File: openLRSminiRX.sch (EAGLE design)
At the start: 19 parts, among them U1 ATMEGA328P, U2 V_REG_LDOSMD

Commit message: update, fully routed.
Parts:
- removed C4, C9: (no value), rcl:C-EUC0805
- removed U2: V_REG_LDOSMD, SparkFun-PowerIC:V_REG_LDOSMD
- added FILTER-1: LFCN-490, minicircuits:LFCN-490
- added IC1: MCP1703CB, linear:MCP1703CB
- added JP10: SCL, SparkFun-Connectors:M01PTH
- added JP11: VCC, SparkFun-Connectors:M01PTH
- added JP12: SBUS, SparkFun-Connectors:M01PTH
- added JP13, JP14, JP8: GND, SparkFun-Connectors:M01PTH
- added JP3: RSSI, SparkFun-Connectors:M01PTH
- added JP4: PPM, SparkFun-Connectors:M01PTH
- added JP5: TXD, SparkFun-Connectors:M01PTH
- added JP6: RXD, SparkFun-Connectors:M01PTH
- added JP7: VIN, SparkFun-Connectors:M01PTH
- added JP9: SDA, SparkFun-Connectors:M01PTH
- added R3, R7: (no value), SparkFun-Resistors:RESISTOR0805-RES
- C1, C10, C5, C6: device rcl:C-EUC0805 -> SparkFun-Capacitors:CAP0805
- JP1: value (none) -> ANT; device SparkFun-Connectors:M05PTH -> SparkFun-Connectors:M01PTH
- JP2: value (none) -> ANTF; device SparkFun-Connectors:M05PTH -> SparkFun-Connectors:M01PTH
- R1, R2, R4, R5, R6: device rcl:R-EU_R0805 -> SparkFun-Resistors:RESISTOR0805-RES
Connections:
- removed net DTR: C9.1
- removed net N$16: C4.1, U2.BP
- new net N$1: FILTER-1.RFIN, JP1.1, U$1.ANT
- new net N$4: FILTER-1.RFOUT, JP2.1
- new net N$5: JP4.1, R7.1
- net GND: now also FILTER-1.GND@2, FILTER-1.GND@4, JP13.1, JP14.1, JP8.1; no longer C4.2, U2.GND
- net N$10: now also R3.2
- net N$18: no longer C9.2
- net PPM: now also R7.2
- net RSSI: now also JP3.1
- net RXD: now also JP6.1
- net SBUS: now also JP12.1
- net SCL: now also JP10.1; no longer JP2.2
- net SDA: now also JP9.1; no longer JP2.3
- net TXD: now also JP5.1
- net VCC: now also IC1.VO, JP11.1, R3.1; no longer JP2.1, U2.OUT
- net VIN: now also IC1.VI, JP7.1; no longer U2.EN, U2.IN
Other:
- moved on the sheet: C1, C10, C5, C6

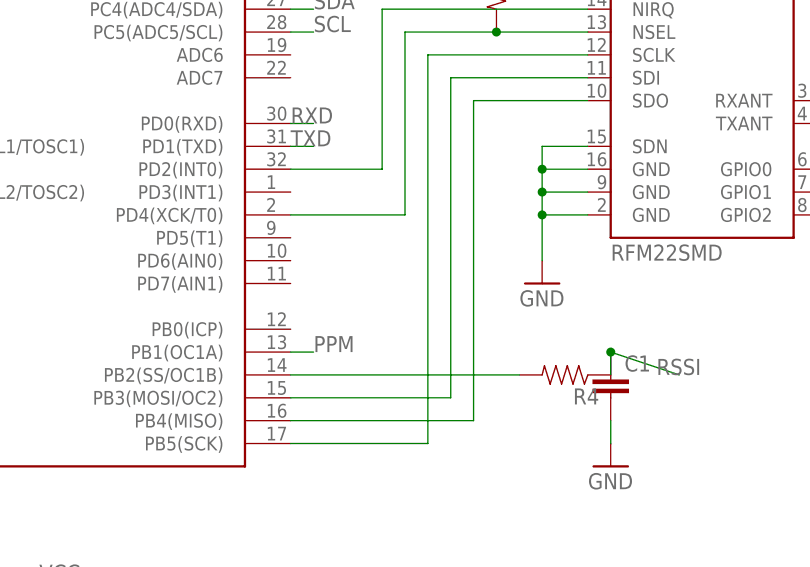
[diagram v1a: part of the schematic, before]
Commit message: updates (fix RSSI output pin)
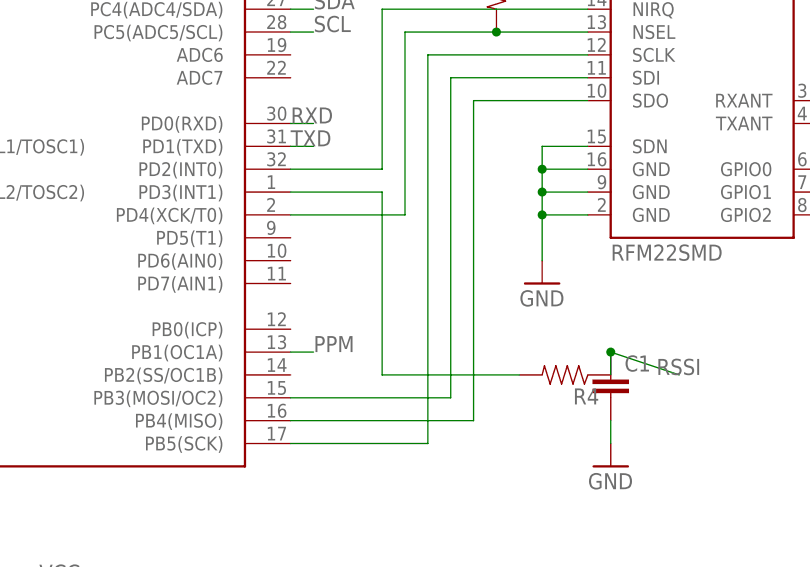
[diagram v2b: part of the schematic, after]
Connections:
- removed net N$17: R4.2, U1.PB2(SS/OC1B)
- new net N$6: R4.2, U1.PD3(INT1)
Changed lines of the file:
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@@
 <?xml version="1.0" encoding="utf-8"?>
 <!DOCTYPE eagle SYSTEM "eagle.dtd">
-<eagle version="6.4">
+<eagle version="6.5.0">
 <drawing>
 <settings>
@@
 </segment>
 </net>
-<net name="N$17" class="0">
-<segment>
-<pinref part="R4" gate="G$1" pin="2"/>
-<pinref part="U1" gate="G$1" pin="PB2(SS/OC1B)"/>
-<wire x1="101.6" y1="35.56" x2="76.2" y2="35.56" width="0.1524" layer="91"/>
-</segment>
-</net>
 <net name="DTR" class="0">
 <segment>
@@
 </segment>
 </net>
+<net name="N$6" class="0">
+<segment>
+<pinref part="R4" gate="G$1" pin="2"/>
+<wire x1="101.6" y1="35.56" x2="86.36" y2="35.56" width="0.1524" layer="91"/>
+<wire x1="86.36" y1="35.56" x2="86.36" y2="55.88" width="0.1524" layer="91"/>
+<pinref part="U1" gate="G$1" pin="PD3(INT1)"/>
+<wire x1="86.36" y1="55.88" x2="76.2" y2="55.88" width="0.1524" layer="91"/>
+</segment>
+</net>

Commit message: cleanups
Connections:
- net GND: now also IC1.GND
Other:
- moved on the sheet: C10, R3
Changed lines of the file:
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@@
 <instance part="R1" gate="G$1" x="83.82" y="101.6" rot="R90"/>
 <instance part="GND1" gate="1" x="104.14" y="45.72"/>
-<instance part="P+1" gate="VCC" x="104.14" y="88.9"/>
+<instance part="P+1" gate="VCC" x="104.14" y="93.98"/>
 <instance part="GND2" gate="1" x="22.86" y="25.4"/>
 <instance part="LED1" gate="G$1" x="83.82" y="91.44" rot="R180"/>
@@
 <instance part="R5" gate="G$1" x="22.86" y="81.28" rot="R270"/>
 <instance part="P+3" gate="VCC" x="17.78" y="81.28"/>
-<instance part="C10" gate="G$1" x="22.86" y="68.58" rot="R180"/>
-<instance part="GND8" gate="1" x="22.86" y="63.5"/>
+<instance part="C10" gate="G$1" x="22.86" y="71.12" rot="R180"/>
+<instance part="GND8" gate="1" x="22.86" y="60.96"/>
 <instance part="Q1" gate="G$1" x="-7.62" y="7.62" rot="MR0"/>
 <instance part="R6" gate="G$1" x="-2.54" y="12.7"/>
@@
 <instance part="JP14" gate="G$1" x="-40.64" y="30.48"/>
 <instance part="GND11" gate="1" x="154.94" y="55.88"/>
-<instance part="R3" gate="G$1" x="99.06" y="78.74" rot="R270"/>
+<instance part="R3" gate="G$1" x="99.06" y="83.82" rot="R270"/>
 <instance part="R7" gate="G$1" x="7.62" y="48.26"/>
 </instances>
@@
 <wire x1="-33.02" y1="30.48" x2="-20.32" y2="30.48" width="0.1524" layer="91"/>
 <wire x1="-20.32" y1="30.48" x2="-20.32" y2="33.02" width="0.1524" layer="91"/>
+<junction x="-20.32" y="33.02"/>
 </segment>
 <segment>
@@
 <wire x1="2.54" y1="96.52" x2="2.54" y2="99.06" width="0.1524" layer="91"/>
 <pinref part="GND4" gate="1" pin="GND"/>
+<pinref part="IC1" gate="G$1" pin="GND"/>
 </segment>
 <segment>
@@
 <pinref part="P+1" gate="VCC" pin="VCC"/>
 <wire x1="109.22" y1="81.28" x2="104.14" y2="81.28" width="0.1524" layer="91"/>
-<wire x1="104.14" y1="81.28" x2="104.14" y2="83.82" width="0.1524" layer="91"/>
+<wire x1="104.14" y1="81.28" x2="104.14" y2="88.9" width="0.1524" layer="91"/>
 <pinref part="R3" gate="G$1" pin="1"/>
-<wire x1="104.14" y1="83.82" x2="104.14" y2="86.36" width="0.1524" layer="91"/>
-<wire x1="99.06" y1="83.82" x2="104.14" y2="83.82" width="0.1524" layer="91"/>
-<junction x="104.14" y="83.82"/>
+<wire x1="104.14" y1="88.9" x2="104.14" y2="91.44" width="0.1524" layer="91"/>
+<wire x1="99.06" y1="88.9" x2="104.14" y2="88.9" width="0.1524" layer="91"/>
+<junction x="104.14" y="88.9"/>
 </segment>
 <segment>
@@
 <wire x1="88.9" y1="73.66" x2="99.06" y2="73.66" width="0.1524" layer="91"/>
 <pinref part="R3" gate="G$1" pin="2"/>
+<wire x1="99.06" y1="78.74" x2="99.06" y2="73.66" width="0.1524" layer="91"/>
 <wire x1="99.06" y1="73.66" x2="109.22" y2="73.66" width="0.1524" layer="91"/>
 <junction x="99.06" y="73.66"/>
@@
 <segment>
 <pinref part="R4" gate="G$1" pin="1"/>
-<wire x1="111.76" y1="38.1" x2="119.38" y2="35.56" width="0.1524" layer="91"/>
-<label x="116.84" y="35.56" size="1.778" layer="95"/>
+<wire x1="111.76" y1="38.1" x2="119.38" y2="38.1" width="0.1524" layer="91"/>
+<label x="119.38" y="38.1" size="1.778" layer="95"/>
 <pinref part="C1" gate="G$1" pin="1"/>
 <junction x="111.76" y="38.1"/>
@@
 </segment>
 </net>
-<net name="DTR" class="0">
-<segment>
-<wire x1="15.24" y1="86.36" x2="12.7" y2="86.36" width="0.1524" layer="91"/>
-</segment>
-</net>
 <net name="N$18" class="0">
 <segment>
@@
 <pinref part="C10" gate="G$1" pin="2"/>
 <pinref part="U1" gate="G$1" pin="AREF"/>
-<wire x1="22.86" y1="71.12" x2="27.94" y2="73.66" width="0.1524" layer="91"/>
+<wire x1="22.86" y1="73.66" x2="27.94" y2="73.66" width="0.1524" layer="91"/>
 <wire x1="27.94" y1="73.66" x2="27.94" y2="71.12" width="0.1524" layer="91"/>
 </segment>

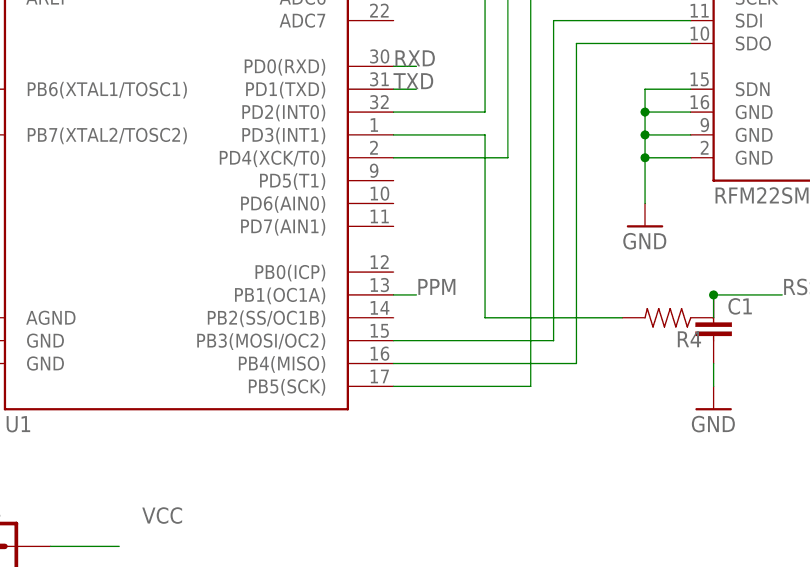
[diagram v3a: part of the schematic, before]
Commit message: Connect ICP to PPM (allow TX operation like on 6ch)
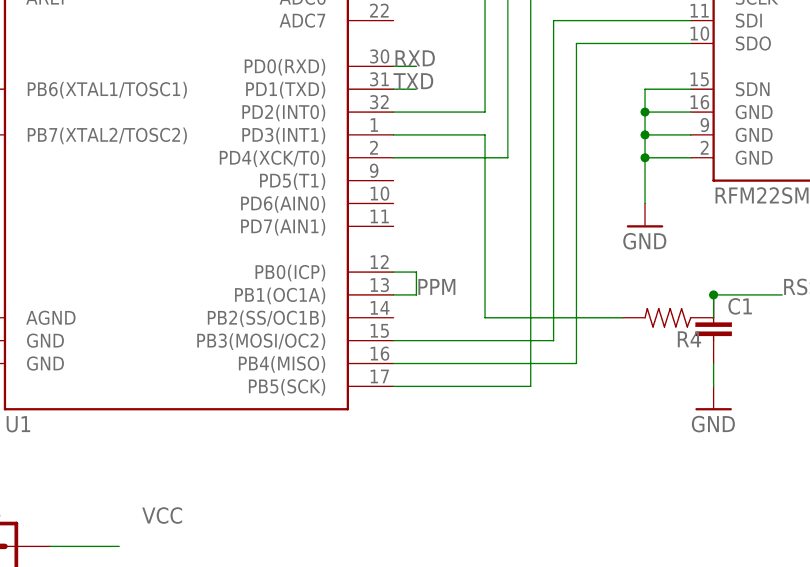
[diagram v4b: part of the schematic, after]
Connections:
- net PPM: now also U1.PB0(ICP)
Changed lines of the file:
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@@
 <wire x1="76.2" y1="38.1" x2="78.74" y2="38.1" width="0.1524" layer="91"/>
 <label x="78.74" y="38.1" size="1.778" layer="95"/>
+<pinref part="U1" gate="G$1" pin="PB0(ICP)"/>
+<wire x1="76.2" y1="40.64" x2="78.74" y2="40.64" width="0.1524" layer="91"/>
+<wire x1="78.74" y1="40.64" x2="78.74" y2="38.1" width="0.1524" layer="91"/>
 </segment>
 <segment>

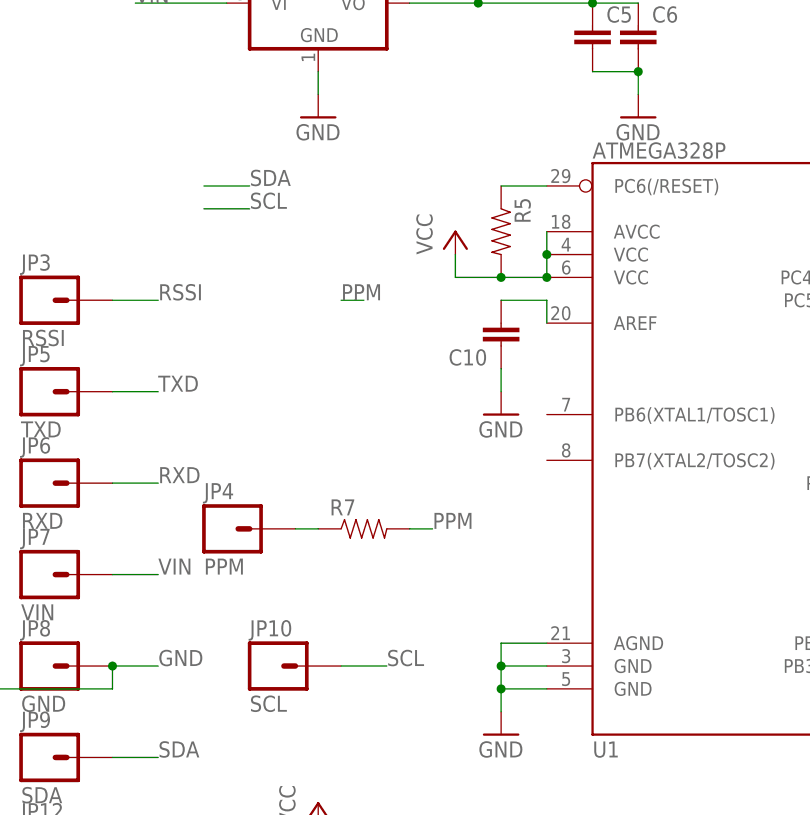
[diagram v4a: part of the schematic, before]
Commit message: add resonator (optional)
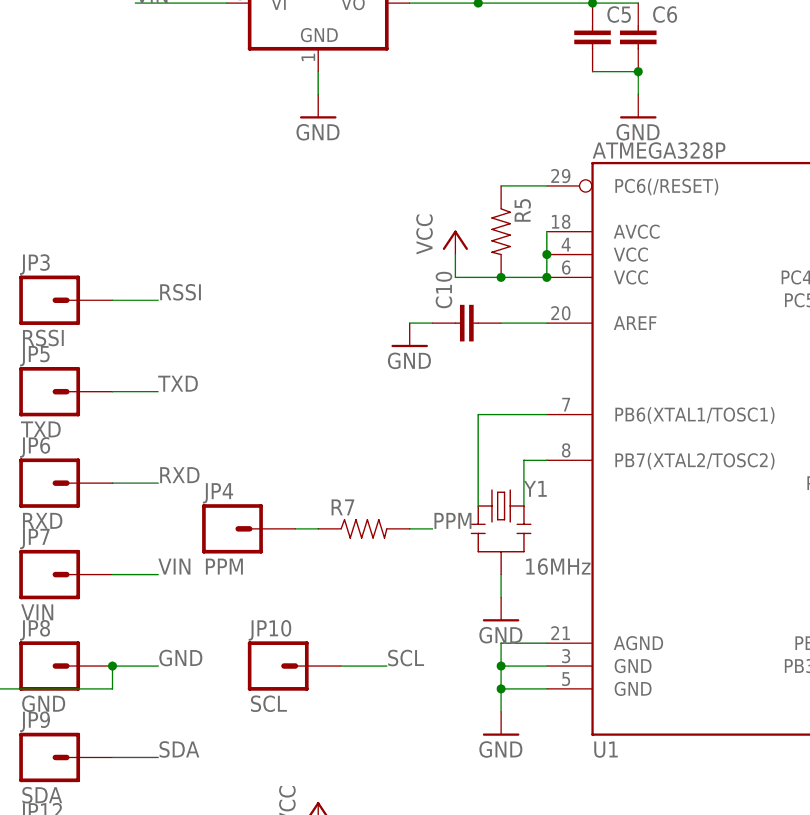
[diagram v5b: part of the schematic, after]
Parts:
- added Y1: 16MHz, SparkFun-FreqCtrl:RESONATOR16MHZ
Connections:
- new net N$16: U1.PB6(XTAL1/TOSC1), Y1.1
- new net N$17: U1.PB7(XTAL2/TOSC2), Y1.3
- net GND: now also Y1.2
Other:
- moved on the sheet: C10
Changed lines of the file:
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@@
 <part name="R3" library="SparkFun-Resistors" deviceset="RESISTOR" device="0805-RES"/>
 <part name="R7" library="SparkFun-Resistors" deviceset="RESISTOR" device="0805-RES"/>
+<part name="Y1" library="SparkFun-FreqCtrl" deviceset="RESONATOR" device="16MHZ" value="16MHz"/>
+<part name="GND12" library="supply1" deviceset="GND" device=""/>
 </parts>
 <sheets>
@@
 <instance part="R5" gate="G$1" x="22.86" y="81.28" rot="R270"/>
 <instance part="P+3" gate="VCC" x="17.78" y="81.28"/>
-<instance part="C10" gate="G$1" x="22.86" y="71.12" rot="R180"/>
-<instance part="GND8" gate="1" x="22.86" y="60.96"/>
+<instance part="C10" gate="G$1" x="20.32" y="71.12" rot="R90"/>
+<instance part="GND8" gate="1" x="12.7" y="68.58"/>
 <instance part="Q1" gate="G$1" x="-7.62" y="7.62" rot="MR0"/>
 <instance part="R6" gate="G$1" x="-2.54" y="12.7"/>
@@
 <instance part="R3" gate="G$1" x="99.06" y="83.82" rot="R270"/>
 <instance part="R7" gate="G$1" x="7.62" y="48.26"/>
+<instance part="Y1" gate="G$1" x="22.86" y="50.8"/>
+<instance part="GND12" gate="1" x="22.86" y="38.1"/>
 </instances>
 <busses>
@@
 <pinref part="C10" gate="G$1" pin="1"/>
 <pinref part="GND8" gate="1" pin="GND"/>
-<wire x1="22.86" y1="66.04" x2="22.86" y2="63.5" width="0.1524" layer="91"/>
+<wire x1="15.24" y1="71.12" x2="12.7" y2="71.12" width="0.1524" layer="91"/>
 </segment>
 <segment>
@@
 <pinref part="JP13" gate="G$1" pin="1"/>
 <pinref part="GND11" gate="1" pin="GND"/>
+</segment>
+<segment>
+<pinref part="Y1" gate="G$1" pin="2"/>
+<pinref part="GND12" gate="1" pin="GND"/>
+<wire x1="22.86" y1="40.64" x2="22.86" y2="43.18" width="0.1524" layer="91"/>
 </segment>
 </net>
@@
 <net name="PPM" class="0">
 <segment>
-<wire x1="5.08" y1="73.66" x2="7.62" y2="73.66" width="0.1524" layer="91"/>
-<label x="5.08" y="73.66" size="1.778" layer="95"/>
-</segment>
-<segment>
 <pinref part="U1" gate="G$1" pin="PB1(OC1A)"/>
 <wire x1="76.2" y1="38.1" x2="78.74" y2="38.1" width="0.1524" layer="91"/>
@@
 </segment>
 <segment>
-<wire x1="-10.16" y1="86.36" x2="-5.08" y2="86.36" width="0.1524" layer="91"/>
-<label x="-5.08" y="86.36" size="1.778" layer="95"/>
-</segment>
-<segment>
 <wire x1="-20.32" y1="22.86" x2="-15.24" y2="22.86" width="0.1524" layer="91"/>
 <label x="-15.24" y="22.86" size="1.778" layer="95"/>
@@
 </segment>
 <segment>
-<wire x1="-10.16" y1="83.82" x2="-5.08" y2="83.82" width="0.1524" layer="91"/>
-<label x="-5.08" y="83.82" size="1.778" layer="95"/>
-</segment>
-<segment>
 <wire x1="5.08" y1="33.02" x2="10.16" y2="33.02" width="0.1524" layer="91"/>
 <label x="10.16" y="33.02" size="1.778" layer="95"/>
@@
 <pinref part="C10" gate="G$1" pin="2"/>
 <pinref part="U1" gate="G$1" pin="AREF"/>
-<wire x1="22.86" y1="73.66" x2="27.94" y2="73.66" width="0.1524" layer="91"/>
-<wire x1="27.94" y1="73.66" x2="27.94" y2="71.12" width="0.1524" layer="91"/>
+<wire x1="22.86" y1="71.12" x2="27.94" y2="71.12" width="0.1524" layer="91"/>
 </segment>
 </net>
@@
 </segment>
 </net>
+<net name="N$16" class="0">
+<segment>
+<pinref part="Y1" gate="G$1" pin="1"/>
+<wire x1="20.32" y1="50.8" x2="20.32" y2="60.96" width="0.1524" layer="91"/>
+<pinref part="U1" gate="G$1" pin="PB6(XTAL1/TOSC1)"/>
+<wire x1="20.32" y1="60.96" x2="27.94" y2="60.96" width="0.1524" layer="91"/>
+</segment>
+</net>
+<net name="N$17" class="0">
+<segment>
+<pinref part="Y1" gate="G$1" pin="3"/>
+<wire x1="25.4" y1="50.8" x2="25.4" y2="55.88" width="0.1524" layer="91"/>
+<pinref part="U1" gate="G$1" pin="PB7(XTAL2/TOSC2)"/>
+<wire x1="25.4" y1="55.88" x2="27.94" y2="55.88" width="0.1524" layer="91"/>
+</segment>
+</net>

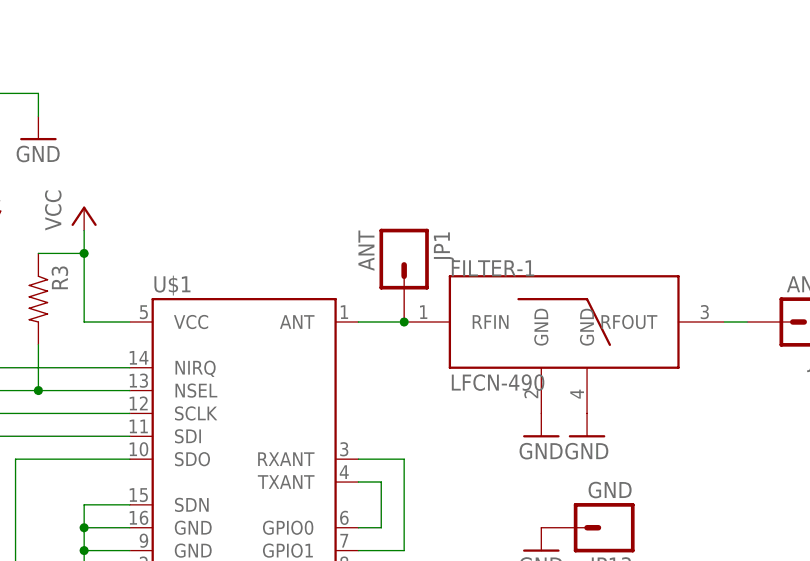
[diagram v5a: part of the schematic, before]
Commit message: Make filtter 'mandatory'. It is still possible to use without filter by soldering to pad directly.
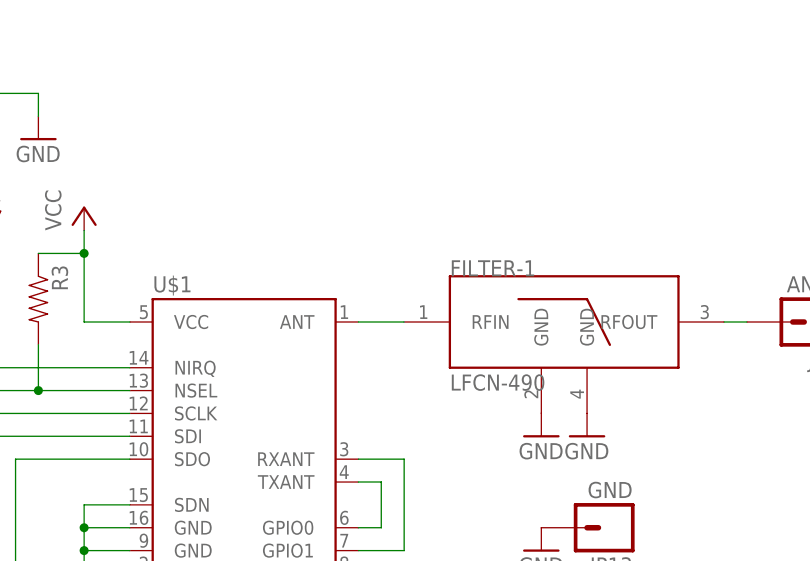
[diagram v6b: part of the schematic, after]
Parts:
- removed JP1: ANT, SparkFun-Connectors:M01PTH
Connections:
- net N$1: no longer JP1.1
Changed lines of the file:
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@@
 <?xml version="1.0" encoding="utf-8"?>
 <!DOCTYPE eagle SYSTEM "eagle.dtd">
-<eagle version="6.5.0">
+<eagle version="6.4">
 <drawing>
 <settings>
@@
 <part name="GND9" library="supply1" deviceset="GND" device=""/>
 <part name="GND10" library="supply1" deviceset="GND" device=""/>
-<part name="JP1" library="SparkFun-Connectors" deviceset="M01" device="PTH" value="ANT"/>
 <part name="JP2" library="SparkFun-Connectors" deviceset="M01" device="PTH" value="ANTF"/>
 <part name="JP3" library="SparkFun-Connectors" deviceset="M01" device="PTH" value="RSSI"/>
@@
 <instance part="GND9" gate="1" x="154.94" y="68.58"/>
 <instance part="GND10" gate="1" x="160.02" y="68.58"/>
-<instance part="JP1" gate="G$1" x="139.7" y="88.9" rot="R270"/>
 <instance part="JP2" gate="G$1" x="185.42" y="81.28" rot="R180"/>
 <instance part="JP3" gate="G$1" x="-27.94" y="73.66"/>
@@
 <pinref part="FILTER-1" gate="G$1" pin="RFIN"/>
 <wire x1="134.62" y1="81.28" x2="139.7" y2="81.28" width="0.1524" layer="91"/>
-<pinref part="JP1" gate="G$1" pin="1"/>
-<junction x="139.7" y="81.28"/>
-</segment>
-</net>
+</segment>
+</net>
